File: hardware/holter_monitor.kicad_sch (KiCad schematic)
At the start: 17 parts, among them J1 USB_C_Receptacle_USB2.0_16P, J2 Conn_01x02, Q1 AO3401A, U1 USBLC6-2SC6, U2 MCP73831-2-OT, U3 AP2112K-3.3

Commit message: Add all elements to KiCad schematic
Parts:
- added C10, C6, C8, C9: 100 nF, Capacitor_SMD:C_0805_2012Metric_Pad1.18x1.45mm_HandSolder, symbol Device:C
- added C5: 22 µF, Capacitor_SMD:C_0805_2012Metric_Pad1.18x1.45mm_HandSolder, symbol Device:C
- added C7: 1 µF, Capacitor_SMD:C_0805_2012Metric_Pad1.18x1.45mm_HandSolder, symbol Device:C
- added D3: LED, LED_SMD:LED_0805_2012Metric_Pad1.15x1.40mm_HandSolder, symbol Device:LED
- added H1, H2, H3, H4: MountingHole, MountingHole:MountingHole_3.2mm_M3, symbol Mechanical:MountingHole
- added J3: Conn_01x06, Connector_PinSocket_2.54mm:PinSocket_1x06_P2.54mm_Vertical, symbol Connector_Generic:Conn_01x06
- added R10, R11, R12, R13: 100kΩ, Resistor_SMD:R_0805_2012Metric_Pad1.20x1.40mm_HandSolder, symbol Device:R
- added R6, R7: 10kΩ, Resistor_SMD:R_0805_2012Metric_Pad1.20x1.40mm_HandSolder, symbol Device:R
- added R8, R9: 1 kΩ, symbol Device:R
- added SW1: SW_SPDT, Button_Switch_THT:SW_Slide_SPDT_Straight_CK_OS102011MS2Q, symbol Switch:SW_SPDT
- added SW2, SW3: SW_Push, Button_Switch_SMD:SW_SPST_TL3342, symbol Switch:SW_Push
- added TP1, TP2, TP3, TP4, TP5, TP6, TP7: TestPoint, TestPoint:TestPoint_Pad_D1.5mm, symbol Connector:TestPoint
- added U4: ESP32-S3-WROOM-1, RF_Module:ESP32-S3-WROOM-1, symbol RF_Module:ESP32-S3-WROOM-1
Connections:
- new net: U4.1 (GND), U4.40 (GND), U4.41 (GND)
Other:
- note added: "Dodatkowe"
- note added: "Dzielnik VBAT"
- note added: "Dzielnik VBUS"
- note added: "Mikrokontroler"
- note added: "Otwory montażowe"
- note added: "Pomiary napięć"
- note added: "Punkty testowe"
- note added: "Tor EKG"
- title: (none) -> Remote ECG signal monitoring system

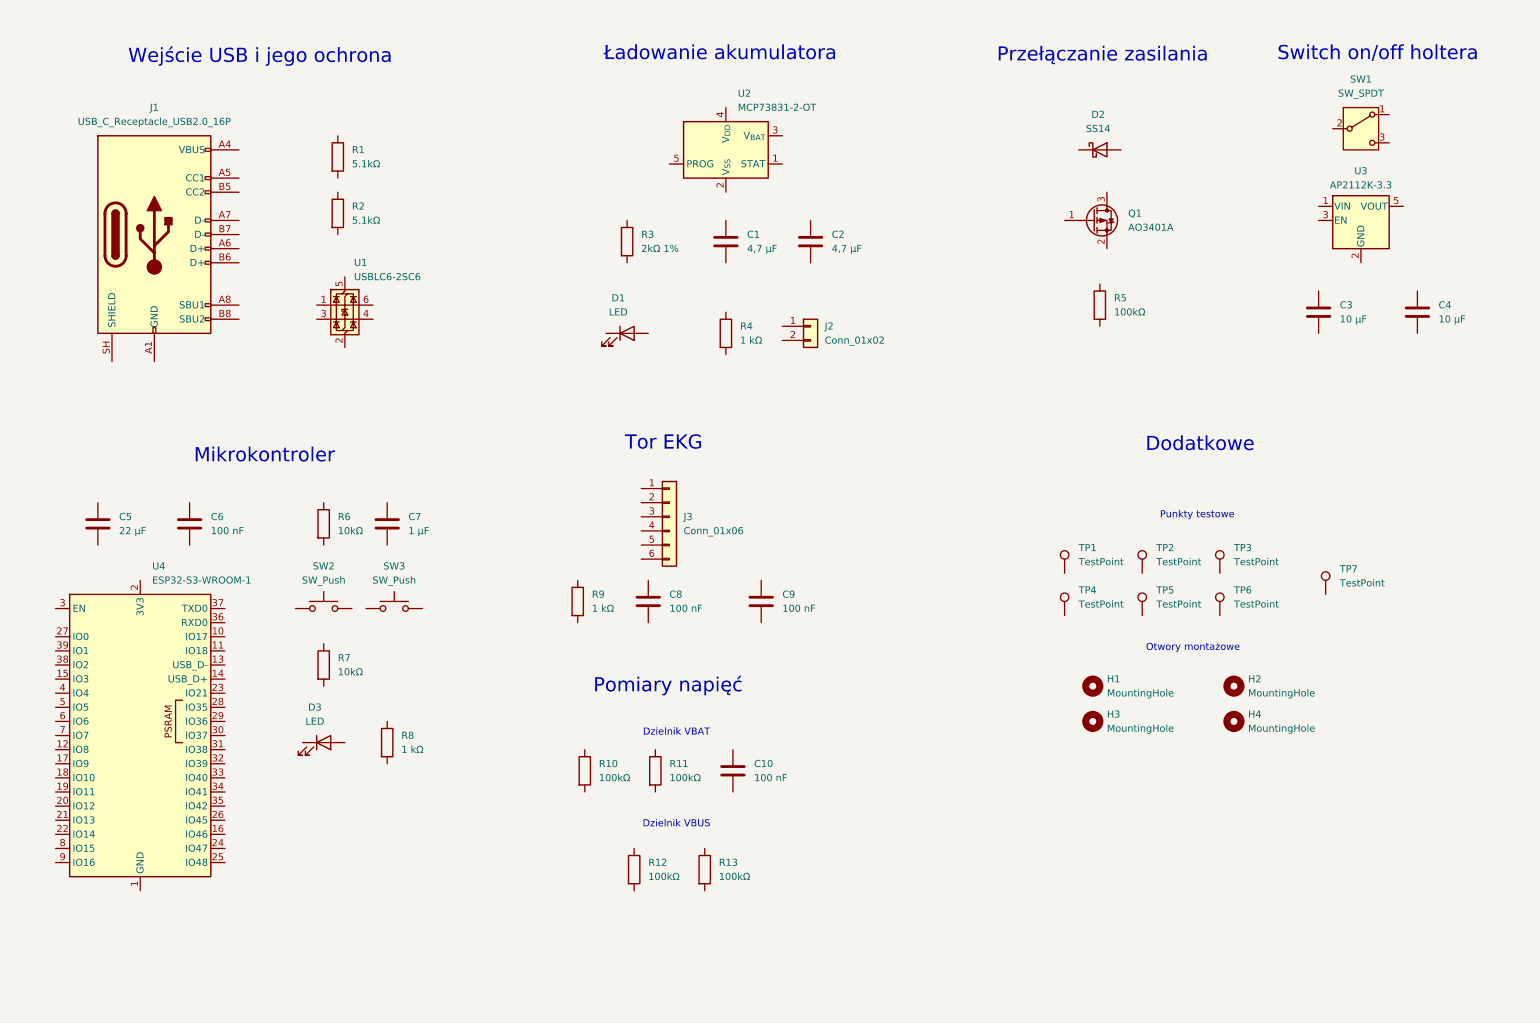
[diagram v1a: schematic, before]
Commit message: Added connections: USB, battery, charging switch, on/off switch, ESP-32-S3, ECG
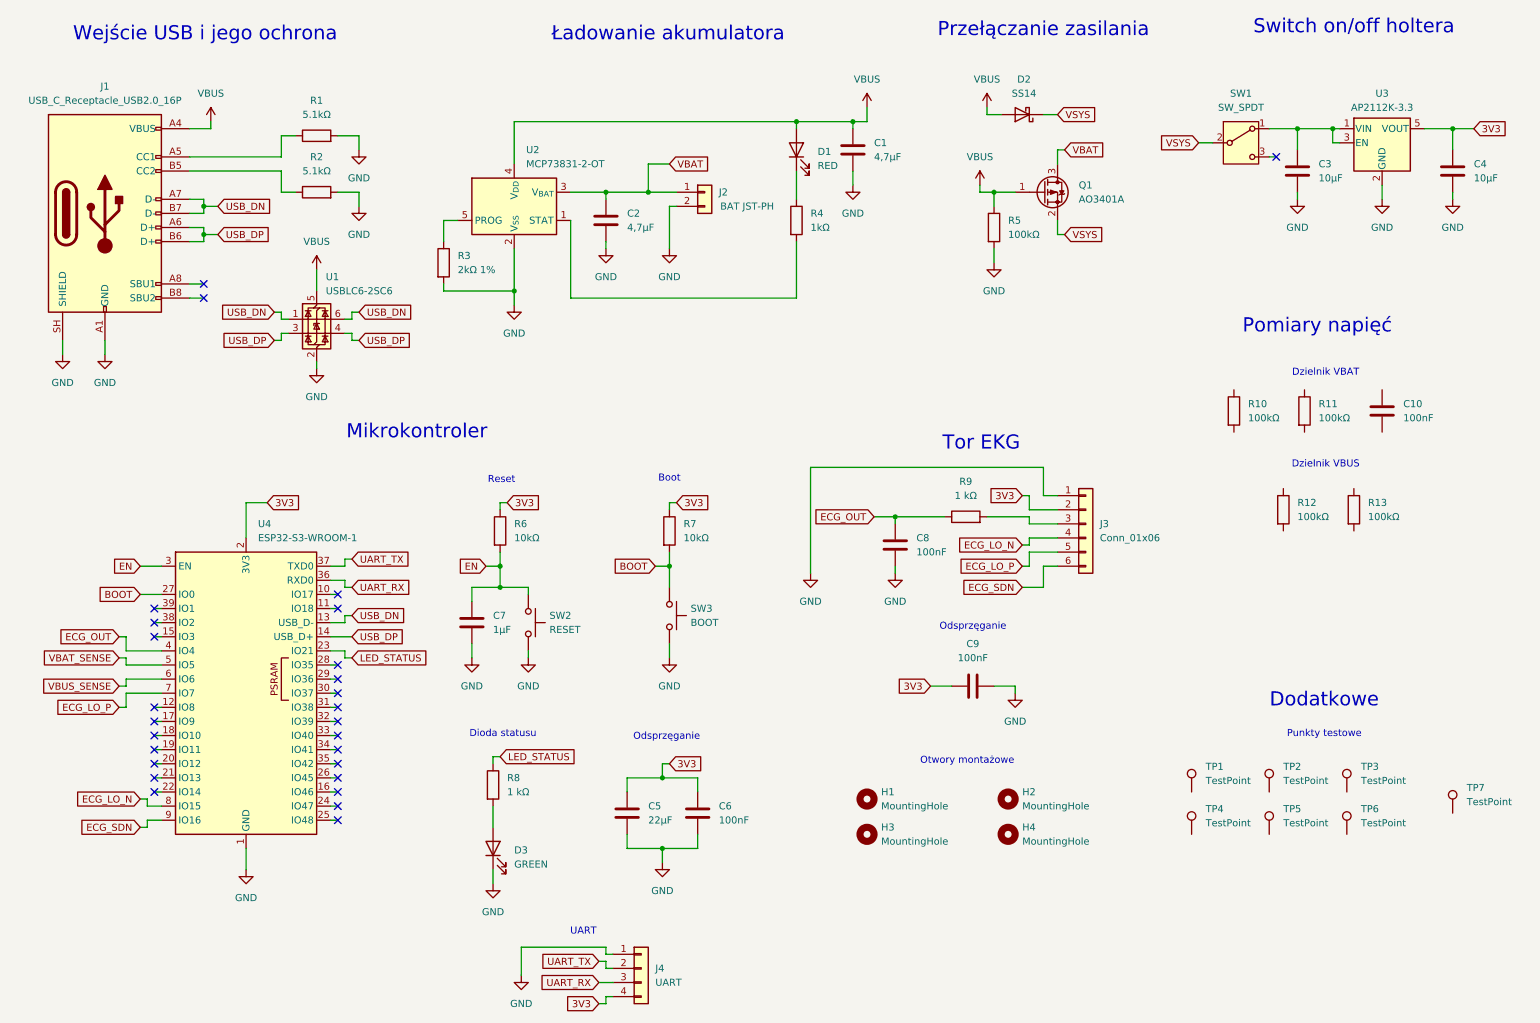
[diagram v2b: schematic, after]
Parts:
- added J4: UART, Connector_PinHeader_2.54mm:PinHeader_1x04_P2.54mm_Vertical, symbol Connector_Generic:Conn_01x04
- C1, C2: value 4,7 µF -> 4,7µF
- C10, C6, C8, C9: value 100 nF -> 100nF
- C3, C4: value 10 µF -> 10µF
- C5: value 22 µF -> 22µF
- C7: value 1 µF -> 1µF
- D1: value LED -> RED
- D3: value LED -> GREEN
- J2: value Conn_01x02 -> BAT JST-PH
- R4: value 1 kΩ -> 1kΩ
- SW2: value SW_Push -> RESET
- SW3: value SW_Push -> BOOT
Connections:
- net 3V3: now reaches C6.1
- net 3V3: now also C4.1, C5.1, C9.1, J3.2 (Pin_2), R6.1, R7.1, U3.5 (VOUT), U4.2 (3V3), J4.4 (Pin_4)
- net GND: now reaches C6.2
- net GND: now also C1.2, C2.2, C3.2, C4.2, C5.2, C7.2, C8.2, C9.2, D3.1 (K), J1.A1 (GND), J1.A12 (GND), J1.B1 (GND), J1.B12 (GND), J1.SH (SHIELD), J2.2 (Pin_2), J3.1 (Pin_1), R1.2, R2.2, R3.2, R5.2, SW2.2, SW3.2, U1.2 (GND), U2.2 (V_{SS}), U3.2 (GND), U4.1 (GND), U4.40 (GND), U4.41 (GND), J4.1 (Pin_1)
- net EN: now reaches R6.2
- net EN: now also C7.1, SW2.1, U4.3 (EN)
- net VBUS: now reaches R5.1
- net VBUS: now also C1.1, D1.2 (A), D2.2 (A), J1.A4 (VBUS), J1.A9 (VBUS), J1.B4 (VBUS), J1.B9 (VBUS), Q1.1 (G), U1.5 (VBUS), U2.4 (V_{DD})
- net USB_DN: now reaches U1.1 (I/O1)
- net USB_DN: now also J1.A7 (D-), J1.B7 (D-), U1.6 (I/O1), U4.13 (USB_D-)
- net USB_DP: now reaches U1.3 (I/O2)
- net USB_DP: now also J1.A6 (D+), J1.B6 (D+), U1.4 (I/O2), U4.14 (USB_D+)
- net at SW1.1 (A): now also C3.1, U3.1 (VIN), U3.3 (EN)
- net VSYS: now reaches SW1.2 (B)
- net VSYS: now also D2.1 (K), Q1.2 (S)
- net ECG_OUT: now reaches C8.1
- net ECG_OUT: now also R9.1, U4.4 (IO4)
- net at R3.1: now also U2.5 (PROG)
- net at R2.1: now also J1.B5 (CC2)
- net VBAT: now reaches C2.1
- net VBAT: now also J2.1 (Pin_1), Q1.3 (D), U2.3 (V_{BAT})
- net BOOT: now reaches R7.2
- net BOOT: now also SW3.1, U4.27 (IO0)
- net at J1.A5 (CC1): now also R1.1
- net at D3.2 (A): now also R8.2
- net at R9.2: now also J3.3 (Pin_3)
- net LED_STATUS: now reaches U4.23 (IO21)
- net LED_STATUS: now also R8.1
- net UART_RX: now reaches U4.36 (RXD0)
- net UART_RX: now also J4.3 (Pin_3)
- net UART_TX: now reaches U4.37 (TXD0)
- net UART_TX: now also J4.2 (Pin_2)
- net VBAT_SENSE: now reaches U4.5 (IO5)
- net VBUS_SENSE: now reaches U4.6 (IO6)
- net ECG_LO_P: now reaches U4.7 (IO7)
- net ECG_LO_P: now also J3.5 (Pin_5)
- net ECG_LO_N: now reaches U4.8 (IO15)
- net ECG_LO_N: now also J3.4 (Pin_4)
- net ECG_SDN: now reaches U4.9 (IO16)
- net ECG_SDN: now also J3.6 (Pin_6)
- net at U2.1 (STAT): now also R4.2
- net at D1.1 (K): now also R4.1
- no-connect marks 0 -> 27
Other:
- note added: "Boot"
- note added: "Dioda statusu"
- note added: "Odsprzęganie"
- note added: "Reset"
- note added: "UART"
- moved on the sheet: C1, C10, C2, C3, C4, C5, C6, C7, C8, C9, D1, D2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

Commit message: Added missing connections
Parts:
- J3: value Conn_01x06 -> AD8232
- R9: value 1 kΩ -> 1kΩ
- TP1: value TestPoint -> TP_VBUS
- TP2: value TestPoint -> TP_VBAT
- TP3: value TestPoint -> TPVSYS
- TP4: value TestPoint -> TP_3V3
- TP5: value TestPoint -> TP_ECG_OUT
- TP6, TP7: value TestPoint -> TP_GND
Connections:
- net 3V3: now also TP4.1
- net ECG_OUT: now also TP5.1
- net GND: now also C10.2, R11.2, R13.2, TP6.1, TP7.1
- net VBAT: now also R10.1, TP2.1
- net VBAT_SENSE: now also C10.1, R10.2, R11.1
- net VBUS: now also R12.1, TP1.1
- net VBUS_SENSE: now also R12.2, R13.1
- net VSYS: now also TP3.1
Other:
- moved on the sheet: C10, C8, C9, H1, H2, H3, H4, J3, R10, R11, R12, R13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

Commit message: Added power flags, resistors and capacitor, fixed erc check fails
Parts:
- added C11: 100nF, Capacitor_SMD:C_0805_2012Metric_Pad1.18x1.45mm_HandSolder, symbol Device:C
- added R14, R15: 22Ω, Resistor_SMD:R_0805_2012Metric_Pad1.20x1.40mm_HandSolder, symbol Device:R
- R4, R8, R9: footprint (none) -> Resistor_SMD:R_0805_2012Metric_Pad1.20x1.40mm_HandSolder
- R5: value 100kΩ -> 10kΩ
- TP3: value TPVSYS -> TP_VSYS
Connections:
- net GND: now also C11.2
- net USB_DN: now also R14.2; no longer J1.A7 (D-), J1.B7 (D-), U1.1 (I/O1), U1.6 (I/O1)
- net USB_DP: now also R15.2; no longer J1.A6 (D+), J1.B6 (D+), U1.3 (I/O2), U1.4 (I/O2)
- net VBUS_SENSE: now also C11.1
- new net: R15.1, U1.4 (I/O2)
- new net: R14.1, U1.6 (I/O1)
- new net USB_CONN_DN: J1.A7 (D-), J1.B7 (D-), U1.1 (I/O1)
- new net USB_CONN_DP: J1.A6 (D+), J1.B6 (D+), U1.3 (I/O2)
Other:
- moved on the sheet: R1, R12, R13, R2, U1
